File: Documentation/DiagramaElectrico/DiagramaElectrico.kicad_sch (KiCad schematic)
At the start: 11 parts, among them M1 Stepper_Motor_bipolar, M2 Stepper_Motor_bipolar, M3 Stepper_Motor_bipolar, M4 Stepper_Motor_bipolar, U1 Motor Driver, U2 NUCLEO64-F411RE, U3 Motor Driver, U4 Motor Driver, U5 Final de Carrera, U7 Final de Carrera, U8 Final de Carrera

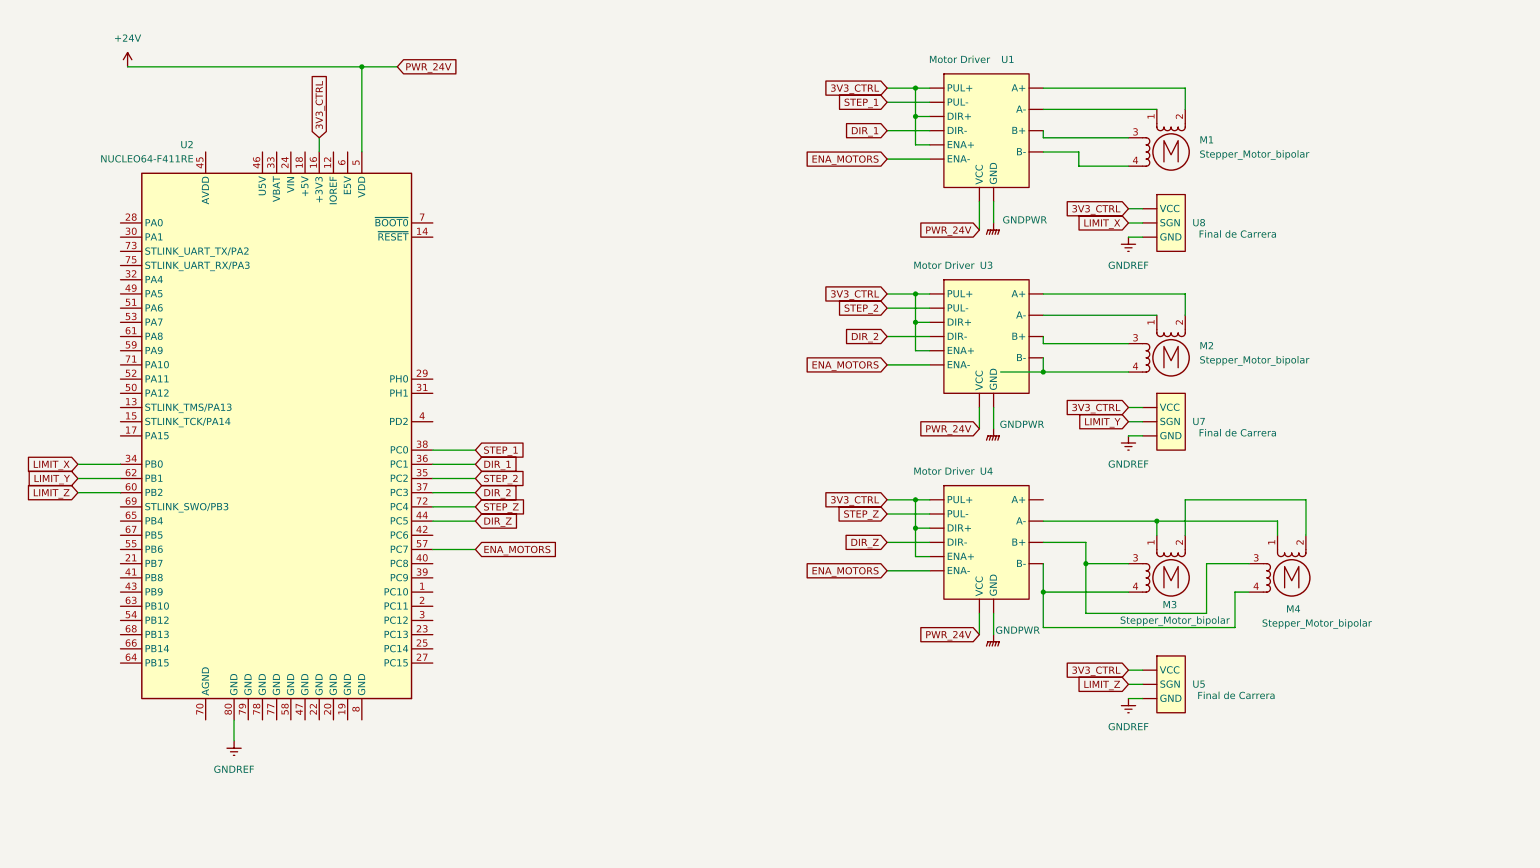
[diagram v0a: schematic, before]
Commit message: Mas esquemas agregados: - Esquematico (a color y blanco&negro) - Diagrama UML
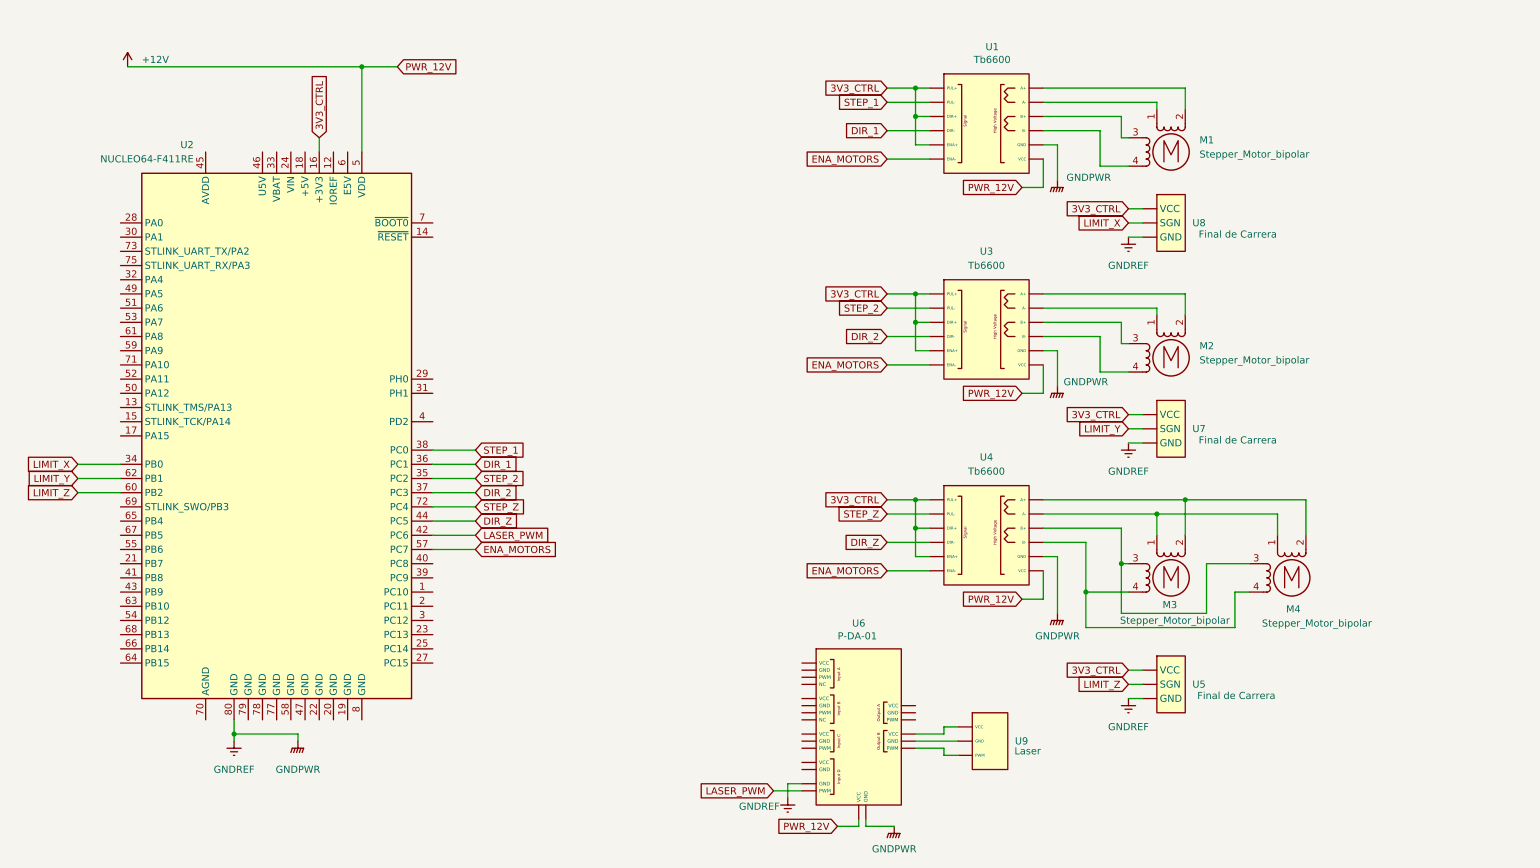
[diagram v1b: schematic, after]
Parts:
- added U6: P-DA-01, symbol TB6600:Driver_Laser
- added U9: Laser, symbol TB6600:Laser
- U1, U3, U4: value Motor Driver -> Tb6600
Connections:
- net GNDPWR: now also U2.80 (GND), U5. (GND), U7. (GND), U8. (GND), U6. (PWM)
- net at M3.2 (-), M4.2 (-): now also U4. (VCC)
- net LASER_PWM: now reaches U2.42 (PC6)
- net LASER_PWM: now also U6. (PWM)
- removed net +24V: U1. (B-), U2.5 (VDD), U3. (B-), U4. (B-)
- removed net GNDREF: U2.80 (GND), U5. (GND), U7. (GND), U8. (GND)
- new net: U6. (PWM), U9. (PWM) (x3)
- new net +12V: U1. (VCC), U2.5 (VDD), U3. (VCC), U4. (VCC), U6. (PWM)
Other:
- moved on the sheet: U7

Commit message: Actualización del README.
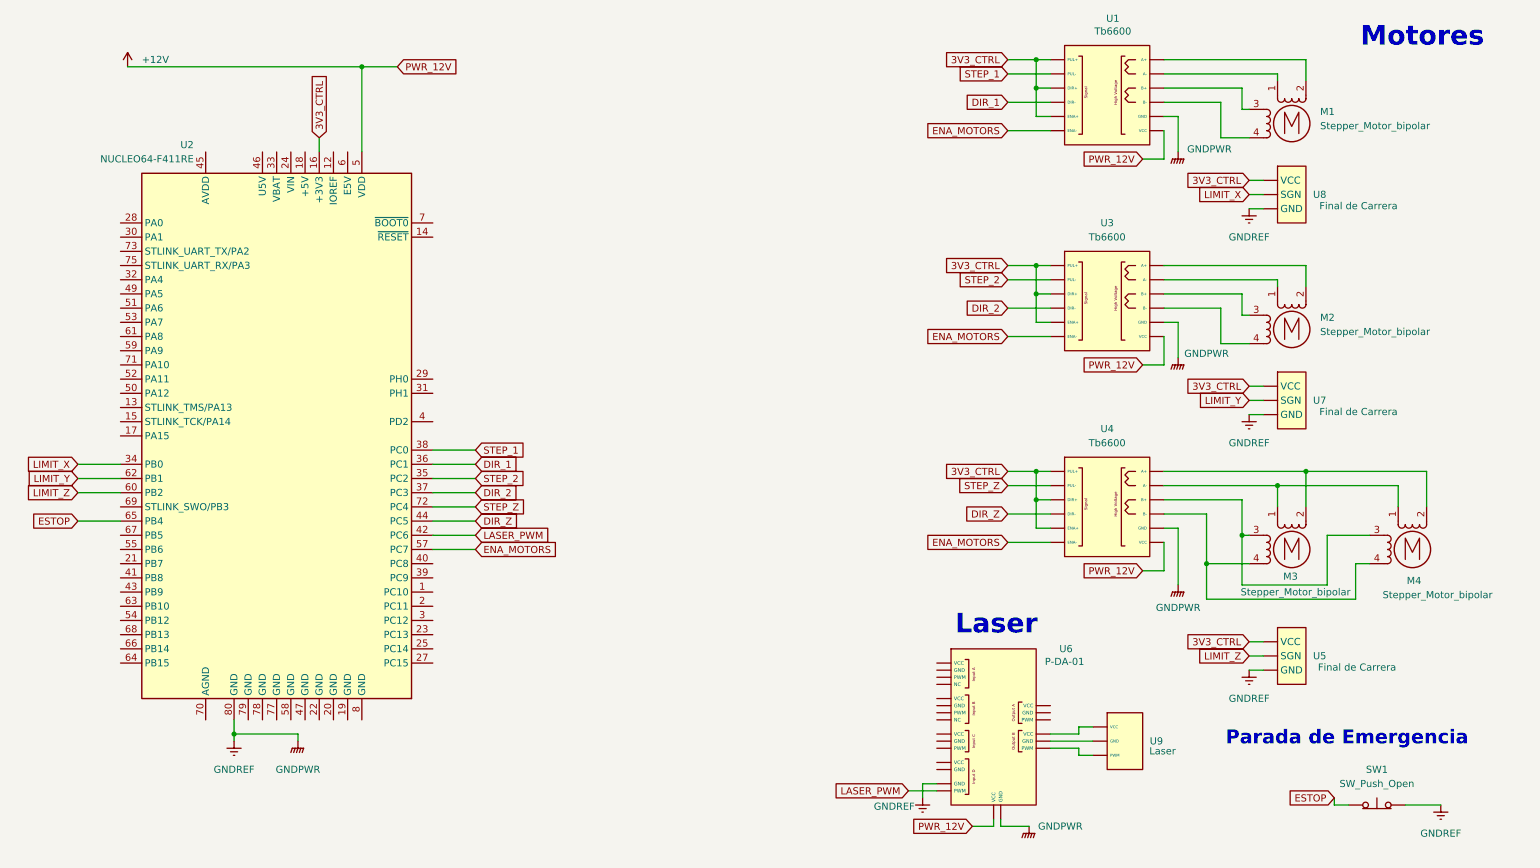
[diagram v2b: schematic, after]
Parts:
- added SW1: SW_Push_Open, symbol Switch:SW_Push_Open
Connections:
- net GNDPWR: now also SW1.2 (B)
- net ESTOP: now reaches U2.65 (PB4)
- net ESTOP: now also SW1.1 (A)
- new net: U6. (PWM), U9. (PWM) (x2)
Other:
- note added: "Laser"
- note added: "Motores"
- note added: "Parada de Emergencia"
- moved on the sheet: M1, M2, M3, M4, U1, U3, U4, U5, U6, U7, U8, U9

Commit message: Se agregan comentarios.
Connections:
- new net: U6. (PWM), U9. (PWM) (x2)
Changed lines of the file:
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@@
 		(title "Esquemático Eléctrico de CNC Laser")
 		(date "2026-10-08")
+		(rev "2026-10-17")
 		(company "Microcontroladores y Electrónica de Potencia - FING - UNCuyo")
 	)
